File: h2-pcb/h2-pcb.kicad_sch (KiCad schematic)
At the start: 54 parts, among them J10 Temp Sensor Conn 3, J11 Actuator Connector 4, J12 Manometer Connector 3, J3 Manometer Connector 1, J4 Manometer Connector 2, J5 Actuator Connector 1, J6 Actuator Connector 2, J7 Actuator Connector 3, J8 Temp Sensor Conn 1, J9 Temp Sensor Conn 2, Q1 NMOS, Q2 PMOS, Q3 NMOS, Q4 PMOS, Q5 NMOS, Q6 PMOS, Q7 NMOS, Q8 PMOS, U4 DS2484

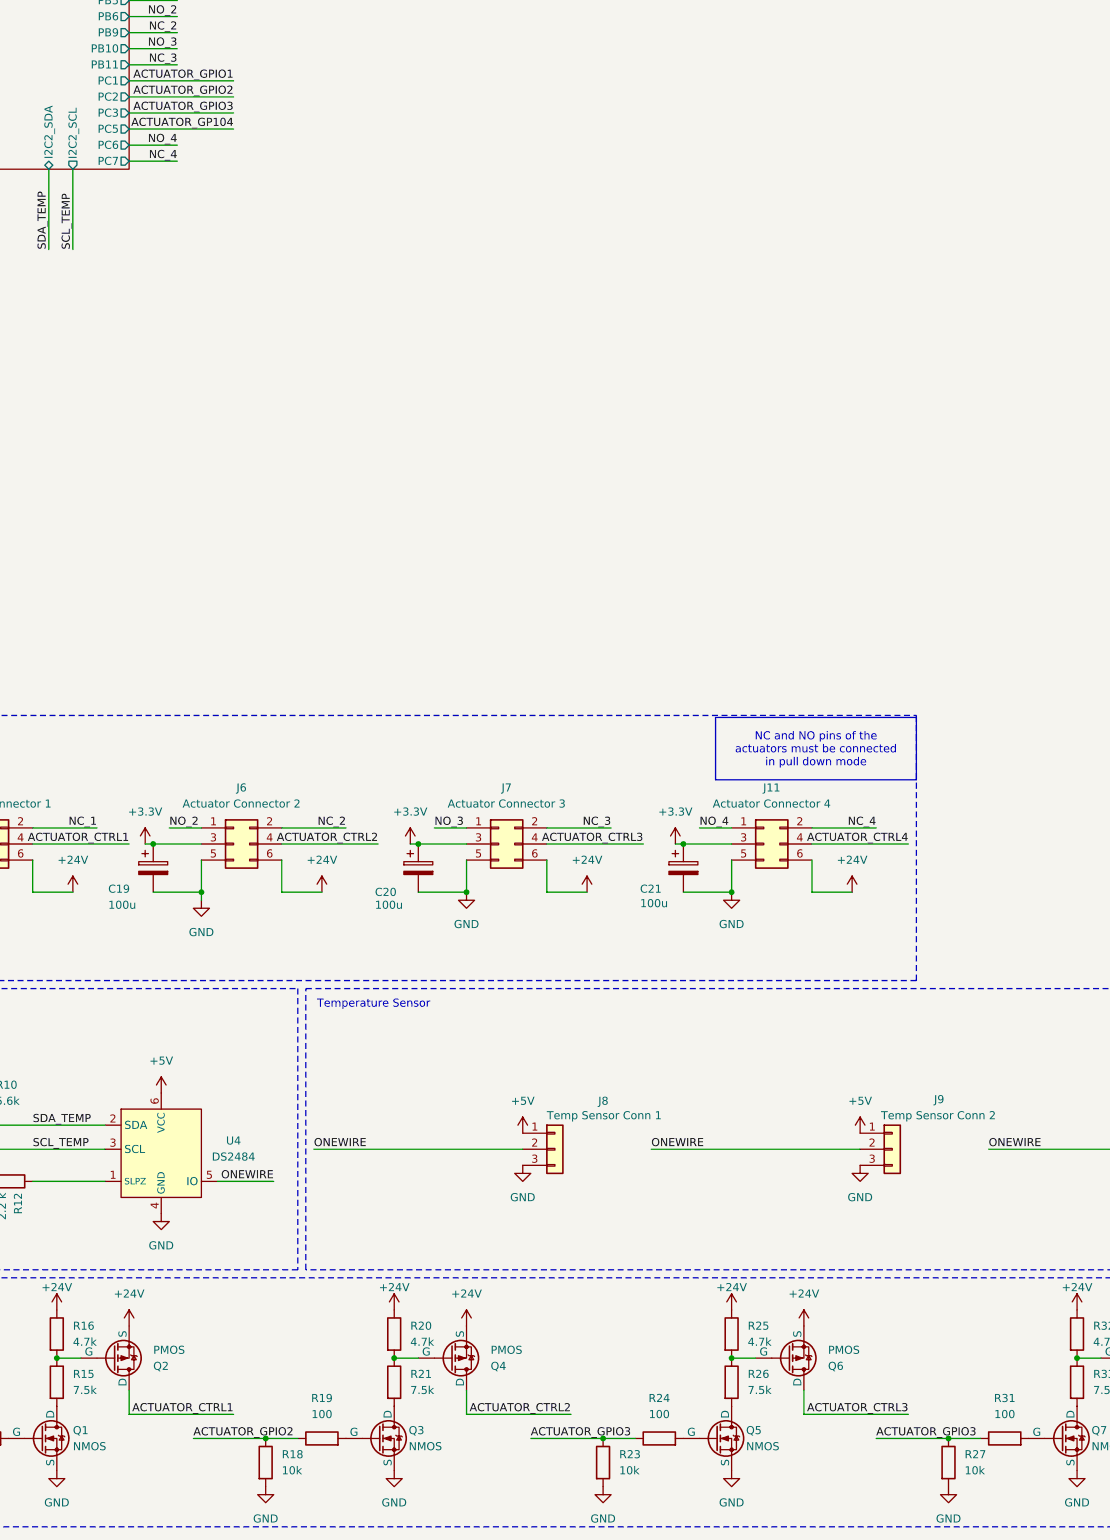
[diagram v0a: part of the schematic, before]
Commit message: Update sur le routage, silkscreen, jlcpcb parts #
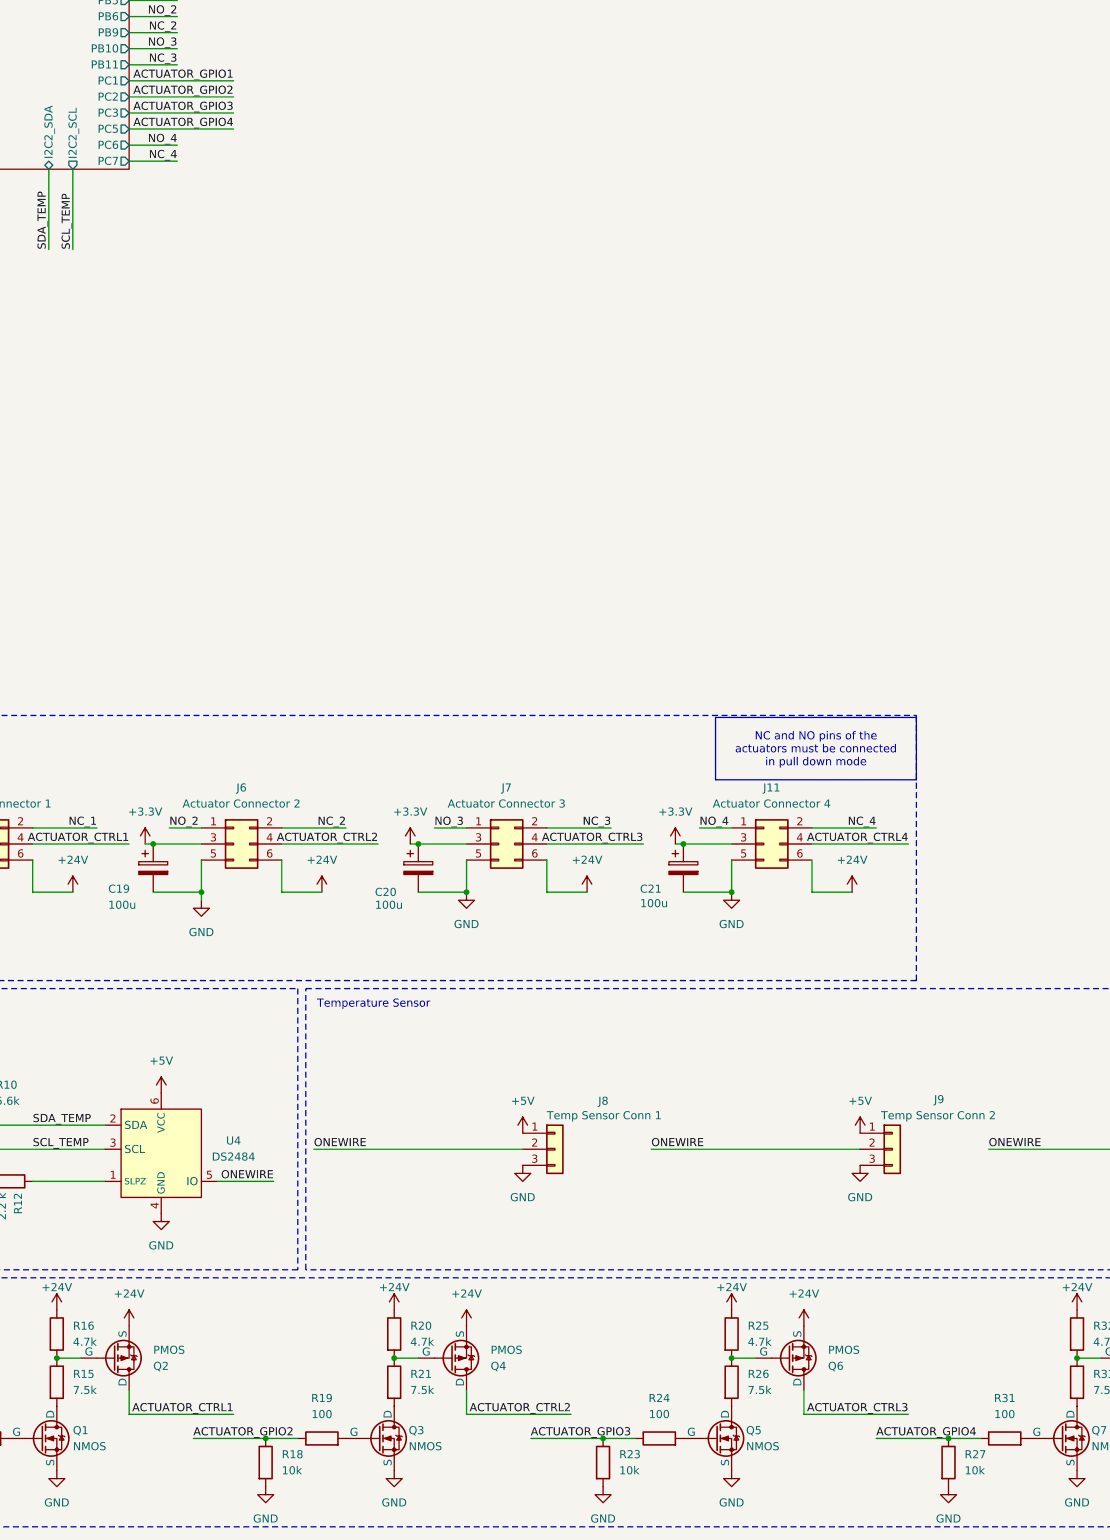
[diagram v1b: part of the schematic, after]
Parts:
- R10, R11: JLCPCB (none) -> C114627
- R12: JLCPCB (none) -> C113303
- U4: JLCPCB (none) -> C2682650
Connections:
- net ACTUATOR_GPIO3: no longer R27.1, R31.1
- new net ACTUATOR_GPIO4: R27.1, R31.1
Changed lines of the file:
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@@
 		)
 	)
-	(label "ACTUATOR_GPIO3"
+	(label "ACTUATOR_GPIO4"
 		(at 176.53 267.97 0)
 		(effects
@@
 		)
 	)
-	(label "ACTUATOR_GP104"
+	(label "ACTUATOR_GPIO4"
 		(at 74.93 60.96 180)
 		(effects
@@
 			)
 		)
-		(property "Datasheet" ""
+		(property "Datasheet" "~"
 			(at 63.5 224.79 0)
 			(effects
@@
 			)
 		)
-		(property "Description" ""
+		(property "Description" "Single-Channel 1-Wire Masterwith Adjustable Timing and Sleep Mode"
 			(at 63.5 224.79 0)
 			(effects
@@
 			)
 		)
+		(property "JLCPCB" "C2682650"
+			(at 63.5 222.25 0)
+			(effects
+				(font
+					(size 1.27 1.27)
+				)
+				(hide yes)
+			)
+		)
 		(pin "6"
 		)
@@
 			)
 		)
+		(property "JLCPCB" "C114627"
+			(at 27.94 213.36 0)
+			(effects
+				(font
+					(size 1.27 1.27)
+				)
+				(hide yes)
+			)
+		)
 		(pin "2"
 		)
@@
 			)
 		)
+		(property "JLCPCB" "C113303"
+			(at 39.37 227.33 0)
+			(effects
+				(font
+					(size 1.27 1.27)
+				)
+				(hide yes)
+			)
+		)
 		(pin "2"
 		)
@@
 			(at 35.56 213.36 0)
 			(effects
+				(font
+					(size 1.27 1.27)
+				)
+				(hide yes)
+			)
+		)
+		(property "JLCPCB" "C114627"
+			(at 35.56 213.36 0)
+			(effects

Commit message: h2-pcb: Fixed DRC errors + cleaned PCB
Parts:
- U4: footprint Exocet:DS2482S-100TR -> (none)
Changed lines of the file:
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@@
 			)
 		)
-		(property "Footprint" "Exocet:DS2482S-100TR"
+		(property "Footprint" ""
 			(at 63.5 224.79 0)
 			(effects
@@
 			)
 		)
-		(property "Datasheet" "~"
+		(property "Datasheet" "https://jlcpcb.com/api/file/downloadByFileSystemAccessId/8586203084079181824"
 			(at 63.5 224.79 0)
 			(effects

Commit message: Footprint to DS24 assigned
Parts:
- U4: footprint (none) -> Exocet:DS2482S-100TR
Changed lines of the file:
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@@
 			)
 		)
-		(property "Footprint" ""
+		(property "Footprint" "Exocet:DS2482S-100TR"
 			(at 63.5 224.79 0)
 			(effects

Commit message: h2-pcb : Added DS2484 footprint
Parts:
- U4: footprint Exocet:DS2482S-100TR -> Package_DFN_QFN:TDFN-8-1EP_3x2mm_P0.5mm_EP1.4x1.4mm
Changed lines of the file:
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@@
 			)
 		)
-		(property "Footprint" "Exocet:DS2482S-100TR"
+		(property "Footprint" "Package_DFN_QFN:TDFN-8-1EP_3x2mm_P0.5mm_EP1.4x1.4mm"
 			(at 63.5 224.79 0)
 			(effects

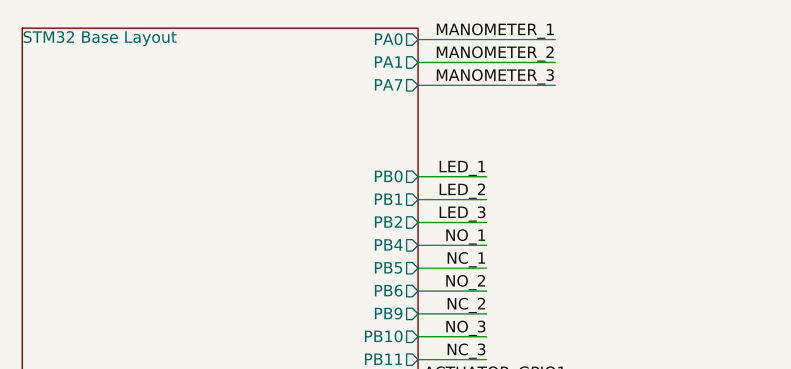
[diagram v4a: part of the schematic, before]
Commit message: h2-pcb: rename PA7 label to PB13
The pin function for PB13 on the MCU was modified, but the hierarchical
label wasn't updated. The one that used to be called "PA7" was renamed
to "PB13" and connected to that pin.

Also updated the routing to refelct these changes.
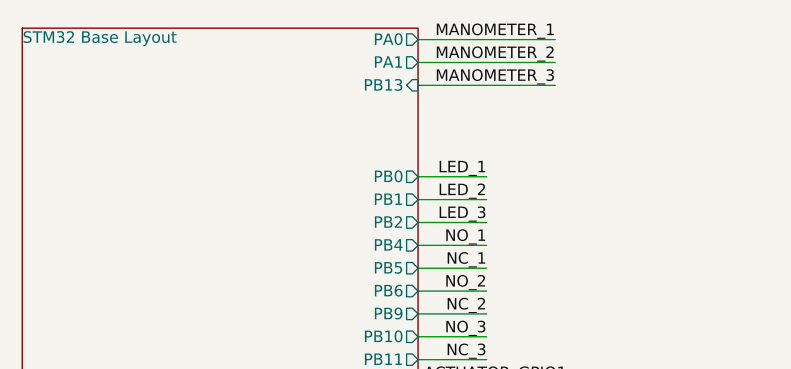
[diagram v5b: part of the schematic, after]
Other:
- sheet STM32 Base Layout ports: added PB13; removed PA7
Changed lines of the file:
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@@
-			)
-		)
-		(pin "PA7" output
-			(at 58.42 20.32 0)
-			(effects
-				(font
-					(size 1.27 1.27)
-				)
-				(justify right)
 			)
 		)
@@
 			)
 		)
+		(pin "PB13" input
+			(at 58.42 20.32 0)
+			(effects
+				(font
+					(size 1.27 1.27)
+				)
+				(justify right)
+			)
+		)

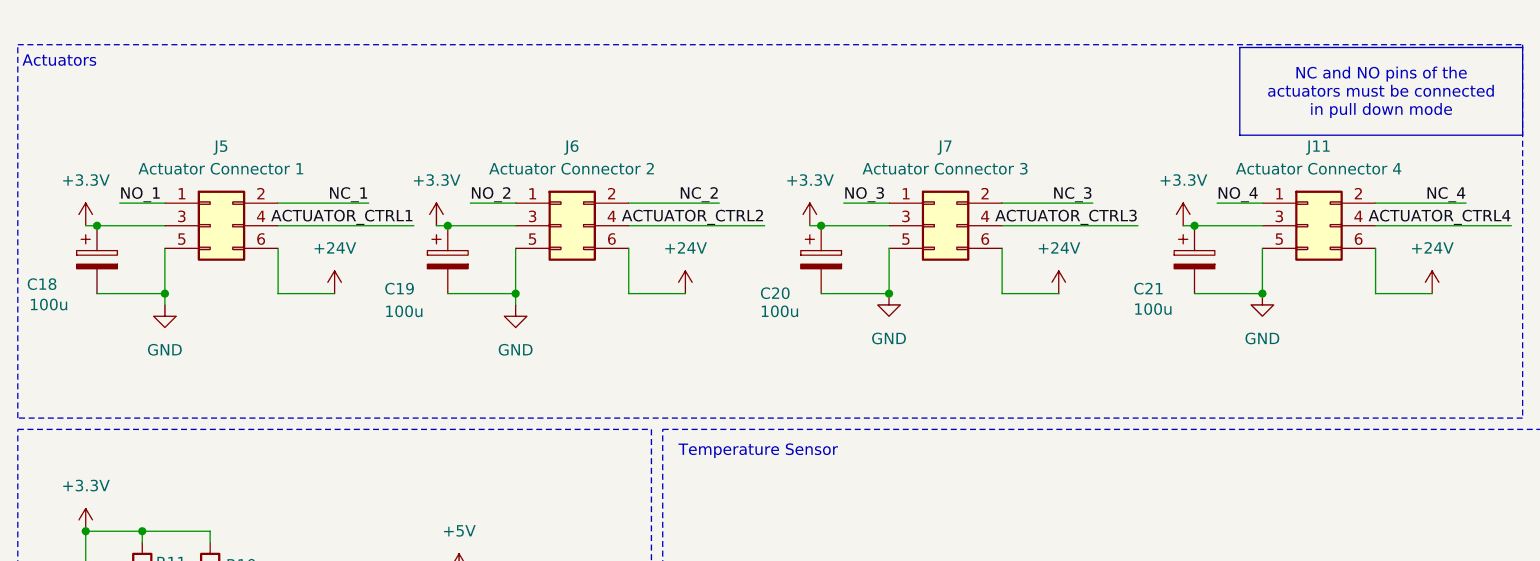
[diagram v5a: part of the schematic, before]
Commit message: h2-pcb: update contactor capacitors
- Changed valued to 10uF
- Changed JLCPCB part
- Connect with +24V instead of +3.3V and update pcb routing
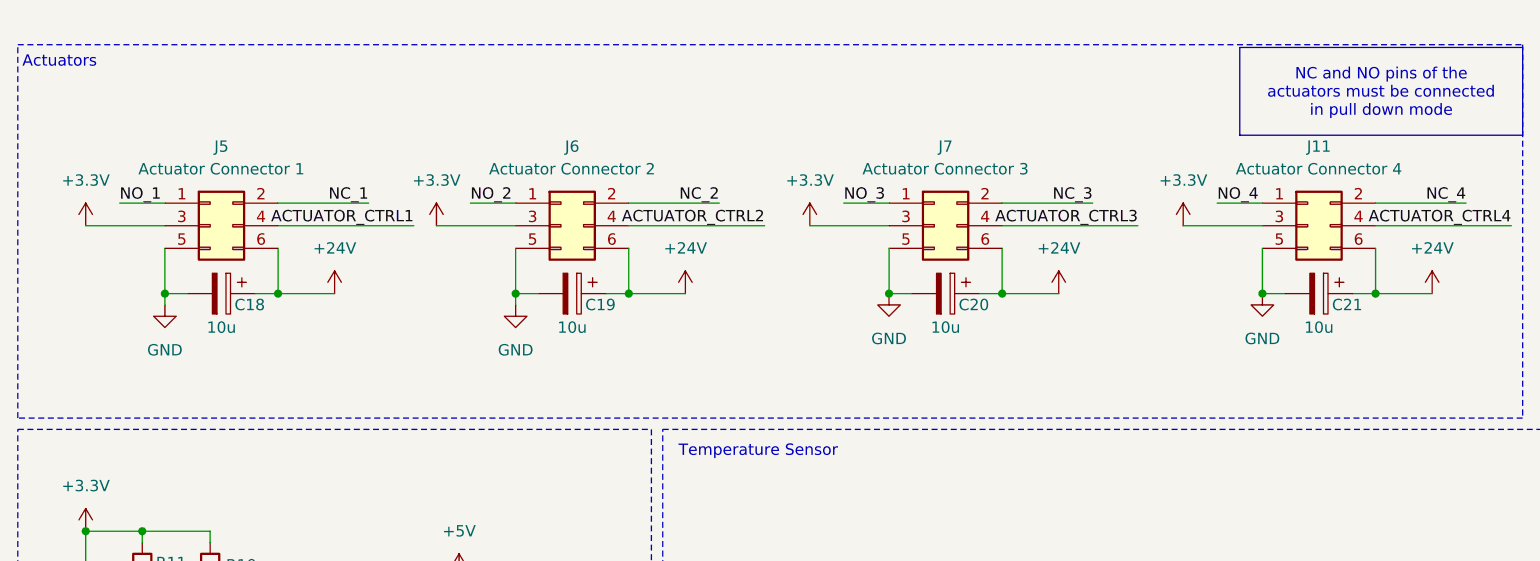
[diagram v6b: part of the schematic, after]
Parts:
- C18, C19, C20, C21: value 100u -> 10u; footprint Capacitor_Tantalum_SMD:CP_EIA-3528-21_Kemet-B -> Capacitor_Tantalum_SMD:CP_EIA-3216-18_Kemet-A; JLCPCB (none) -> C7171
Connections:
- net +24V: now also C18.1, C19.1, C20.1, C21.1
- net +3.3V: no longer C18.1, C19.1, C20.1, C21.1
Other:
- moved on the sheet: C18

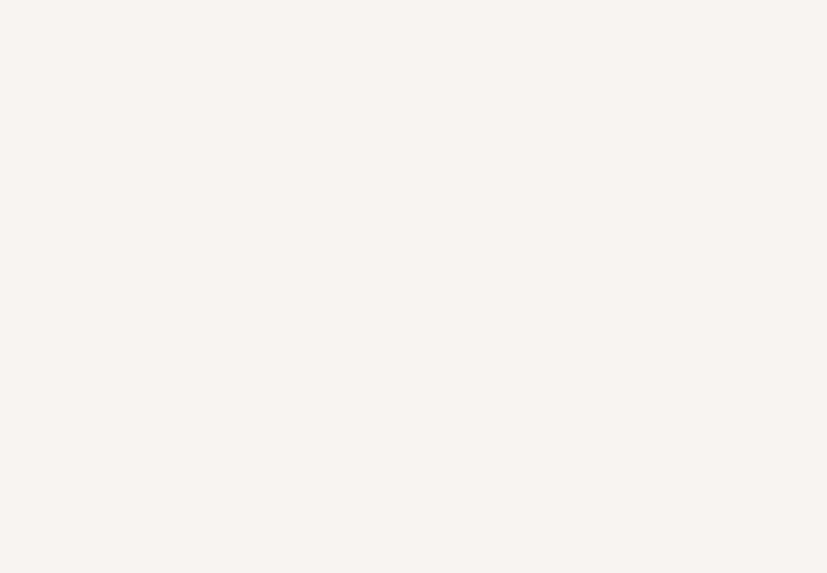
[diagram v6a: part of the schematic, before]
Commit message: h2-pcb: add test points to schematic
- Updated PCB, but not routed yet
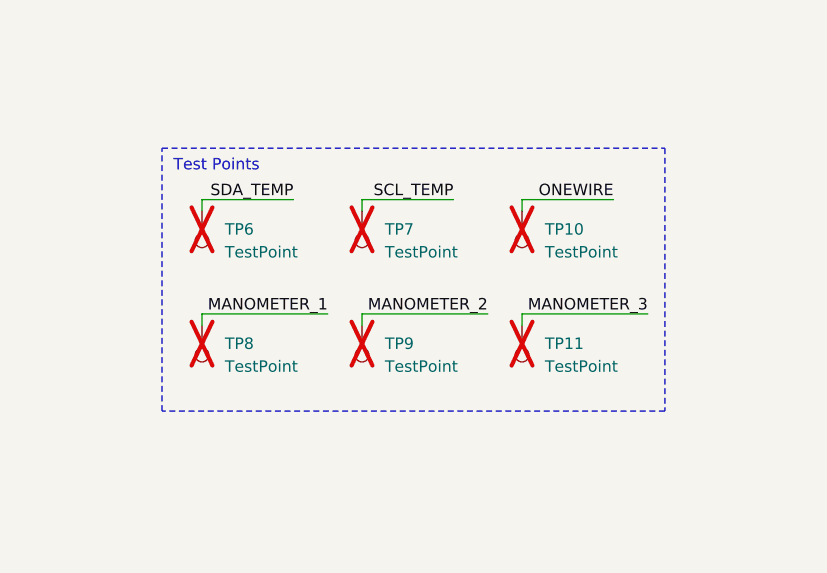
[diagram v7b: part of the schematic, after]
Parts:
- added TP10, TP11, TP6, TP7, TP8, TP9: TestPoint, TestPoint:TestPoint_Keystone_5005-5009_Compact, symbol Connector:TestPoint
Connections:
- net MANOMETER_1: now also TP8.1
- net MANOMETER_2: now also TP9.1
- net MANOMETER_3: now also TP11.1
- net ONEWIRE: now also TP10.1
- net SCL_TEMP: now also TP7.1
- net SDA_TEMP: now also TP6.1
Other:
- note added: "Test Points"
